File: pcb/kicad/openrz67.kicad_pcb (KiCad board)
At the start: 2 copper layers, 48 x 25 mm, 64 parts, among them J1 EXP (not populated), K1 G6K-2F-Y DC3, K2 G6K-2F-Y DC3, Q1 DTC114EKAT146, Q2 DTC114EKAT146, U1 ESP32-C3FH4, U3 LGS5500EP, U4 S4B-XH-A(LF)(SN), X1 40MHz, X2 32.768kHz

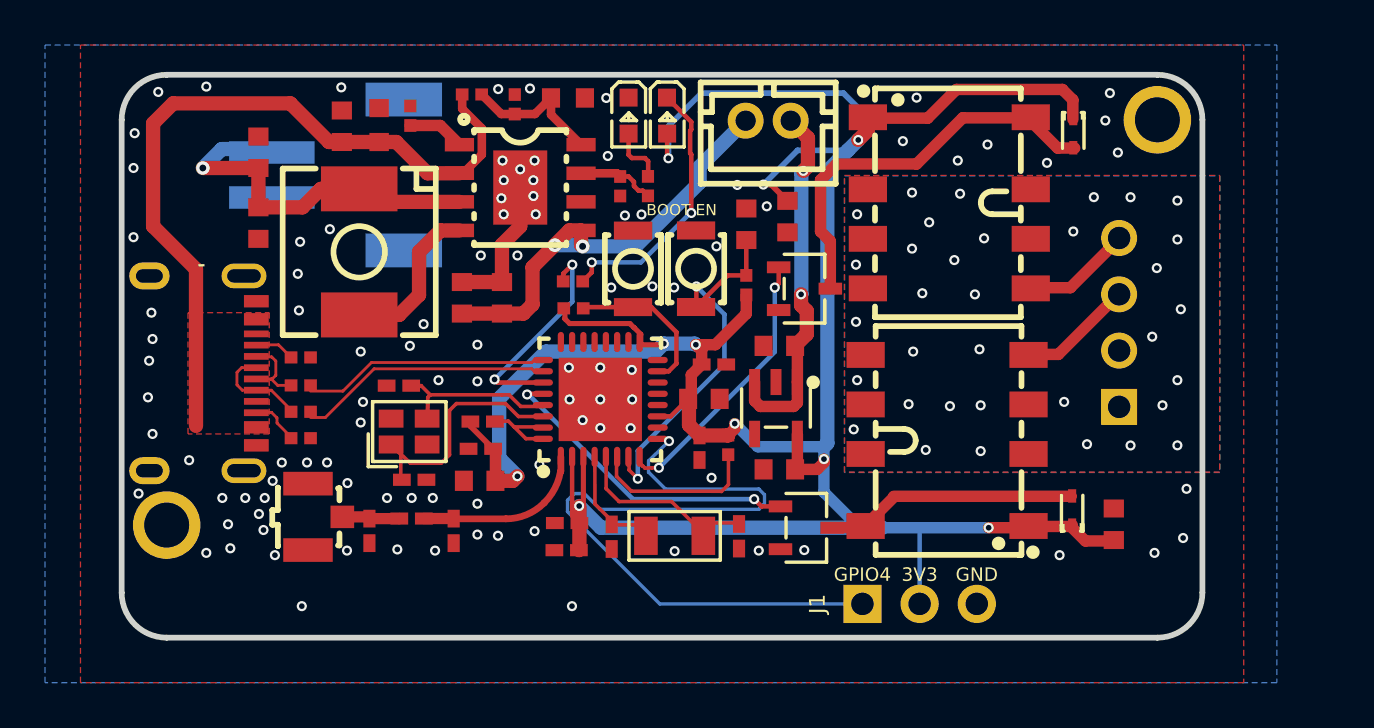
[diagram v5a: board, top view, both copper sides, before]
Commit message: Revert the 25 mm widening and the J1 expansion header
The header cost more than it bought. Reaching the new edge strip forced the
GPIO4 return path across the bottom pour, which split the B.Cu ground under
U1 and LDO1 off into a separate island and displaced three stitching vias
next to the antenna trace. One GPIO, on a header that was not going to be
populated, does not pay for that.

There is no cheap way back either: a through-hole pad needs both layers clear
at the same spot, and on this outline only two isolated positions qualify.
Bottom-side solder pads do fit, but the cell now occupies the bottom. It
belongs in the same pass as the enclosure rework, not before it.

- Board back to 48 x 22 mm; J1, its footprint and the GPIO4 net are gone from
  board, schematic and symbol library.
- B.Cu ground is one region of 649.5 mm2 holding both U1 and LDO1, and the
  antenna trace has 15 GND stitching vias again, the count it had before the
  header.
- Carried forward from 010d742 because they had nothing to do with the header:
  BAT1 sits 0.15 mm further off the board edge, and copper-to-edge 0.3 mm now
  actually reaches the zone filler. Without both, the reverted board fails DRC
  with an edge-clearance error on the BAT1 fixing pad.

Board and schematic hygiene in the same pass:

- Board title block added; the Gerber job file reported revision "rev?" and
  now reports 2.
- BAT+ / BAT- and the polarity mark raised to 1.067 mm, matching the board's
  other silkscreen. Every text now clears JLCPCB's 1.0 mm except the BOOT EN
  label, which cannot be enlarged where it sits; see README.
- BAT1 footprint silkscreen line 0.06 -> 0.15 mm, under the fab minimum.
- Two vias at 0.305 mm drill merged into the 0.300 mm tool: 7 drill tools -> 6.
- ERC is now 0 errors, 0 warnings. Removed an orphan S1/S2/AGND label cluster
  that connected nothing, and shortened three wire tails that ran past their
  labels. Netlist verified node-for-node before and after: 64 nets, identical.
- AGND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
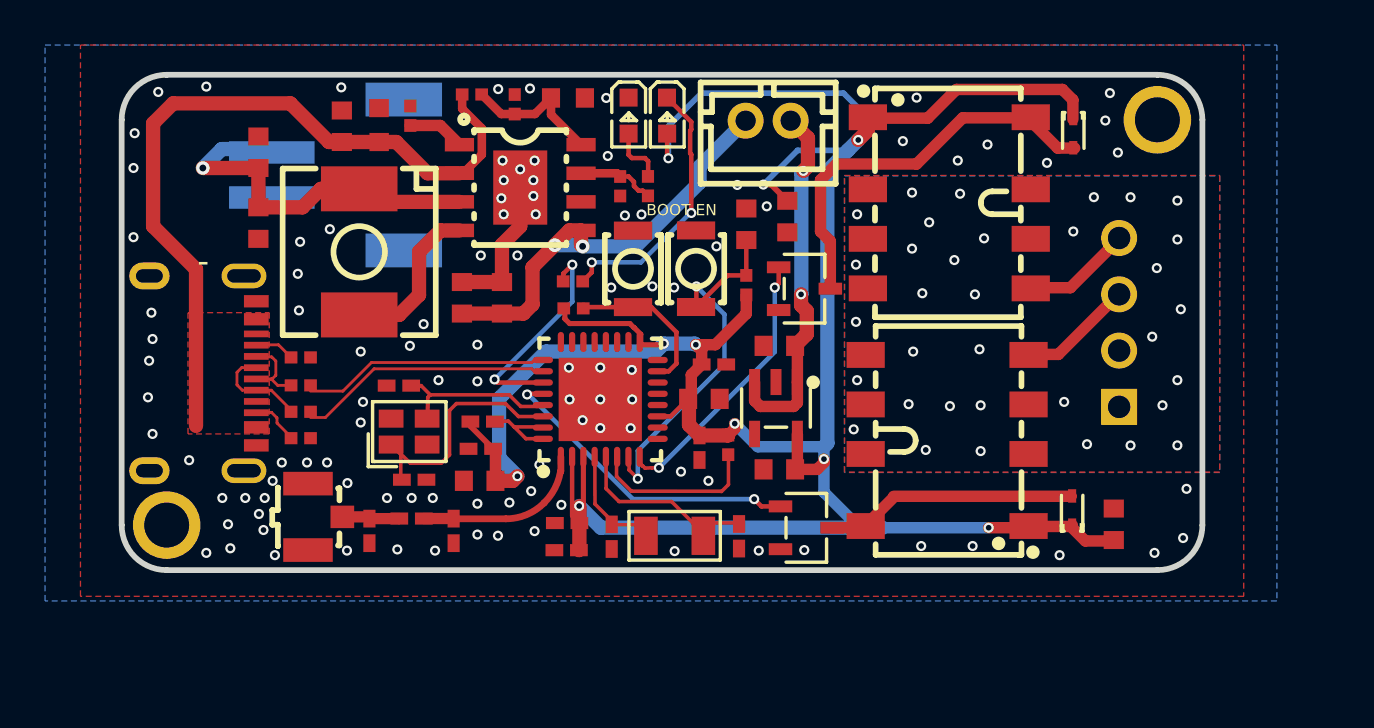
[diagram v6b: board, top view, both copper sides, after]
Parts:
- removed J1: EXP (not populated), openrz67:PinHeader_1x03_P2.54mm_Vertical
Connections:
- U1 pad 9: GPIO4 -> unconnected-(U1-MTMS-Pad9)
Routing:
- net GPIO4: track 32.9 -> 0.00 mm, vias 1 -> 0
- net VCC: track 127.4 -> 124.0 mm
- net GND: vias 100 -> 103
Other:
- board size 48 x 25 mm -> 48 x 22 mm
- board text removed: "3V3"
- board text removed: "GPIO4"

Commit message: Rev 2: decouple the ESP32-C3 analog supply behind the ferrite bead
L2 sits between VCC and U1 pins 31/32 (VDDA, radio and ADC supply), but every
3.3 V capacitor on the board was on the VCC side of it. A bead with no
capacitor behind it is just series impedance: the radio's transmit bursts have
to pull through it, and the noise it is meant to block has no path to ground.
Espressif's reference design puts 0.1 uF at those pins.

Rather than squeeze a new part into the 2 mm gap in front of the pins, reuse
C5, the 100 nF that already sat 1.2 mm from L2 pin 2: move it to the far side
of the bead. The net is now named VDDA.

- Schematic: C5 moved onto the L2 -> U1 wire, global label VDDA on that net.
- Board: C5 pad 1 on VDDA with a 0.16 mm track from L2 pad 2; the four VCC
  segments that fed L2 pin 1 through C5 are gone, replaced by a 0.45/0.25 via
  beside L2 pad 1 down to the existing B.Cu VCC track. B.Cu ground under U1
  stays one region (648.7 mm2).
- Same part, same position: BOM and position file are unchanged.

DRC 0 errors, the same 8 known warnings; schematic parity clean; ERC 0/0.
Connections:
- C5 pad 1: VCC -> VDDA
- L2 pad 2: Net-(L2-Pad2) -> VDDA
- U1 pad 31: Net-(L2-Pad2) -> VDDA
- U1 pad 32: Net-(L2-Pad2) -> VDDA
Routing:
- net VDDA: track 0.00 -> 5.13 mm
- net Net-(L2-Pad2): track 3.92 -> 0.00 mm
- net VCC: track 124.0 -> 122.6 mm, vias 10 -> 11
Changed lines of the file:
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@@
 			(size 0.79 0.54)
 			(layers "F.Cu" "F.Mask" "F.Paste")
-			(net "Net-(L2-Pad2)")
+			(net "VDDA")
 		)
 		(embedded_fonts no)
@@
 			(size 0.79 0.54)
 			(layers "F.Cu" "F.Mask" "F.Paste")
-			(net "VCC")
+			(net "VDDA")
 		)
 		(pad "2" smd rect
@@
 			(size 0.9 0.28)
 			(layers "F.Cu" "F.Mask" "F.Paste")
-			(net "Net-(L2-Pad2)")
+			(net "VDDA")
 		)
 		(pad "32" smd oval
@@
 			(size 0.9 0.28)
 			(layers "F.Cu" "F.Mask" "F.Paste")
-			(net "Net-(L2-Pad2)")
+			(net "VDDA")
 		)
 		(pad "33" smd rect
@@
 	)
 	(segment
-		(start 136.6005 108.034)
-		(end 136.6005 106.7155)
-		(width 0.508)
-		(layer "F.Cu")
-		(net "VCC")
-	)
-	(segment
 		(start 162.801 110.704)
 		(end 162.1565 110.0595)
@@
 	)
 	(segment
-		(start 136.6005 106.7155)
-		(end 136.4965 106.6115)
-		(width 0.508)
-		(layer "F.Cu")
-		(net "VCC")
-	)
-	(segment
 		(start 153.1425 91.926)
 		(end 153.1425 92.4685)
@@
 	)
 	(segment
-		(start 135.487 105.602)
-		(end 136.4965 106.6115)
-		(width 0.254)
-		(layer "F.Cu")
-		(net "VCC")
-	)
-	(segment
 		(start 142.7495 101.227)
 		(end 142.5725 101.0495)
@@
 	)
 	(segment
-		(start 135.487 105.4025)
-		(end 135.487 105.602)
-		(width 0.254)
-		(layer "F.Cu")
-		(net "VCC")
-	)
-	(segment
 		(start 158.5065 110.117)
 		(end 160.204 110.117)
@@
 	)
 	(via
+		(at 135.05 105.4025)
+		(size 0.45)
+		(drill 0.25)
+		(layers "F.Cu" "B.Cu")
+		(net "VCC")
+	)
+	(via
 		(at 144.2825 93.7085)
 		(size 0.45)
@@
 	)
 	(segment
+		(start 135.05 105.4025)
+		(end 136.764 105.4025)
+		(width 0.2)
+		(layer "B.Cu")
+		(net "VCC")
+	)
+	(segment
 		(start 150.0185 93.357)
 		(end 148.499 94.877)
@@
 		(width 0.16)
 		(layer "F.Cu")
-		(net "Net-(L2-Pad2)")
+		(net "VDDA")
 	)
 	(segment
@@
 		(width 0.16)
 		(layer "F.Cu")
-		(net "Net-(L2-Pad2)")
+		(net "VDDA")
+	)
+	(segment
+		(start 136.585 105.4025)
+		(end 136.4965 106.6115)
+		(width 0.16)
+		(layer "F.Cu")
+		(net "VDDA")
 	)
 	(segment
@@
 		(width 0.16)
 		(layer "F.Cu")
-		(net "Net-(L2-Pad2)")
+		(net "VDDA")
 	)
 	(segment
@@
 		(width 0.16)
 		(layer "F.Cu")
-		(net "Net-(L2-Pad2)")
+		(net "VDDA")
 	)
 	(segment
@@
 		(width 0.16)
 		(layer "F.Cu")
-		(net "Net-(L2-Pad2)")
+		(net "VDDA")
 	)
 	(segment
@@
 		(width 0.16)
 		(layer "F.Cu")
-		(net "Net-(L2-Pad2)")
+		(net "VDDA")
 	)
 	(segment

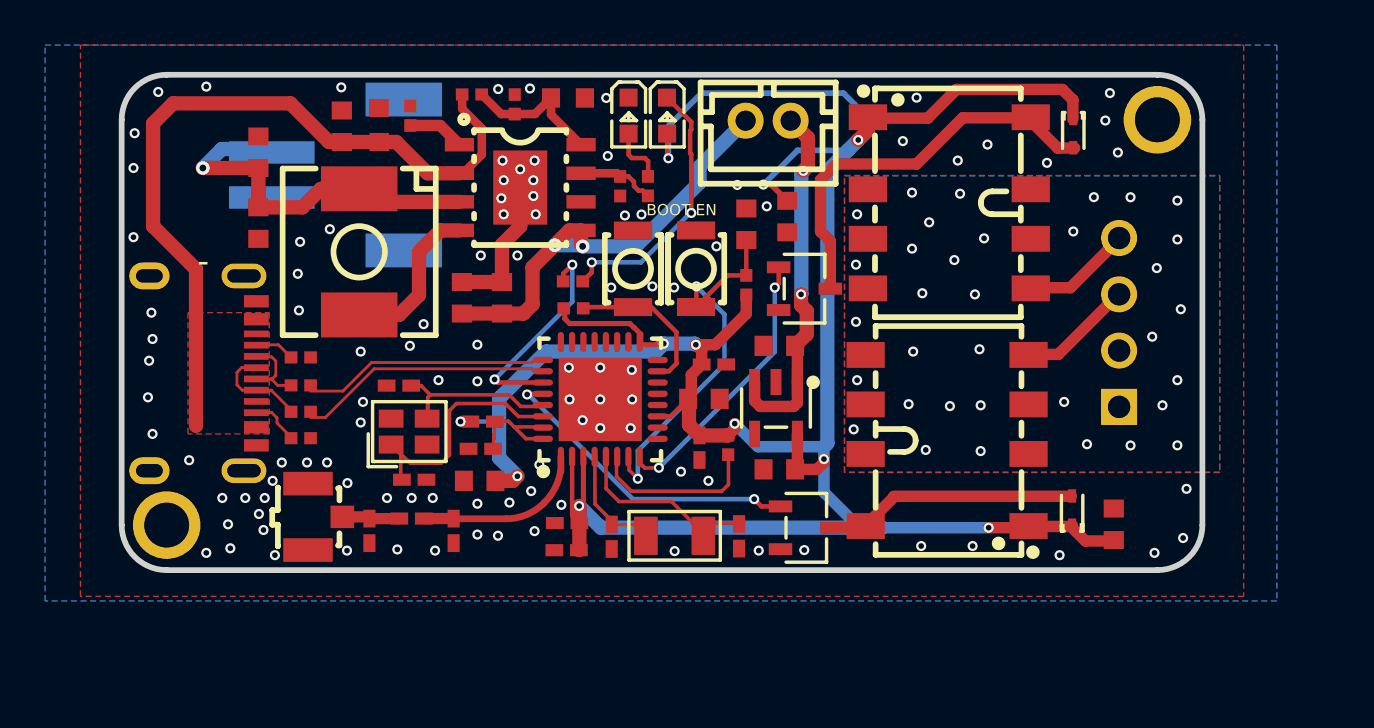
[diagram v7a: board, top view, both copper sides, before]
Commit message: Rev 2: replace the G6K relays with TLP172GM PhotoMOS, fix the JLCPCB CPL format
Each shutter channel is now one Toshiba TLP172GM (LCSC C261926) with its LED
driven from the GPIO through 330 R (C25104). K1/K2, the DTC114E drivers, the
flyback diodes and the coil decoupling caps are gone: eight parts become four,
the tallest top-side part drops from 5.2 to 2.2 mm, and no coil current is
drawn while an exposure is held. Camera ground stays isolated: AGND touches
only U4 pin 2 and the two PhotoMOS outputs, and the AGND pours were pulled in
so the LED side sits in the GND domain.

R4/R5 (USB 22 R) move to UNI-ROYAL 0402WGF220JTCE (C25092, Basic); JLCPCB
had two of the Yageo part in stock.

regen.sh rewrites the position file into JLCPCB's CPL header layout; their
uploader rejects KiCad's native header.

DRC 0 errors / 7 known warnings, ERC 0/0, schematic parity clean.
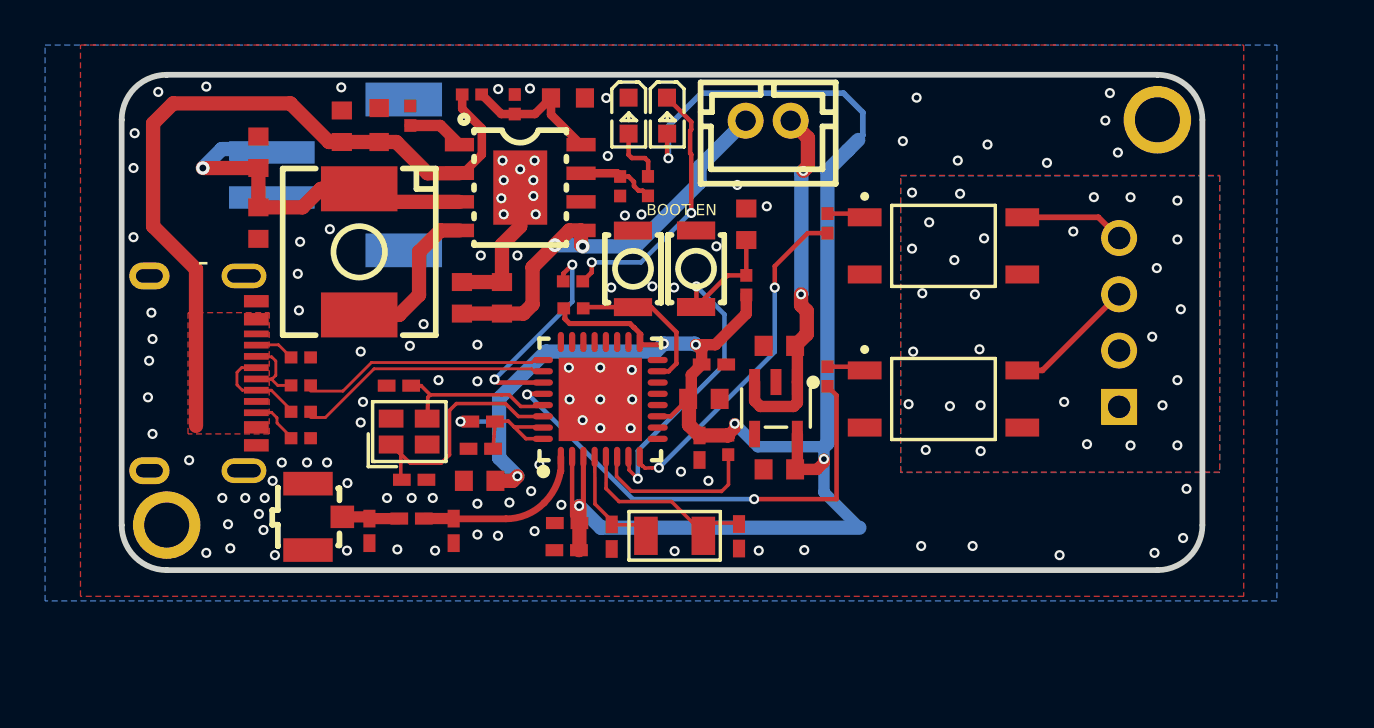
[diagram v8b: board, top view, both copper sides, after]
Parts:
- removed C27, C28: 10uF, openrz67:C0603
- removed D1, D2: 1N4148WT, openrz67:SOD-523_L1.2-W0.8-LS1.6-RD
- removed K1, K2: G6K-2F-Y DC3, openrz67:RELAY-SMD_G6K-2F-Y
- removed Q1, Q2: DTC114EKAT146, openrz67:SOT-346_L2.9-W1.6-P1.90-LS2.8-TR-CW
- added R21: 330Ω, openrz67:R0402, F.Cu at (151.3, 103.4)
- added R22: 330Ω, openrz67:R0402, F.Cu at (151.3, 96.6)
- added U5: TLP172GM, openrz67:SMD-4_L4.6-W3.7-P2.54-LS7.0-BR, F.Cu at (156.5, 104.4)
- added U6: TLP172GM, openrz67:SMD-4_L4.6-W3.7-P2.54-LS7.0-BR, F.Cu at (156.5, 97.6)
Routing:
- net VCC: track 122.6 -> 93.4 mm, vias 11 -> 8
- net Net-(D2-A): track 17.8 -> 0.00 mm
- net Net-(D1-A): track 11.1 -> 0.00 mm
- net D6: track 14.1 -> 21.7 mm
- net D1: track 12.3 -> 15.2 mm
- net Net-(U6-A): track 0.00 -> 1.72 mm
- net Net-(U5-A): track 0.00 -> 1.72 mm
- net S1: track 5.17 -> 5.71 mm
- net AGND: vias 34 -> 29
